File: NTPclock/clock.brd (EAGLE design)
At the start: 115 x 85 mm, 26 parts, among them IC1 MAX7219CNG

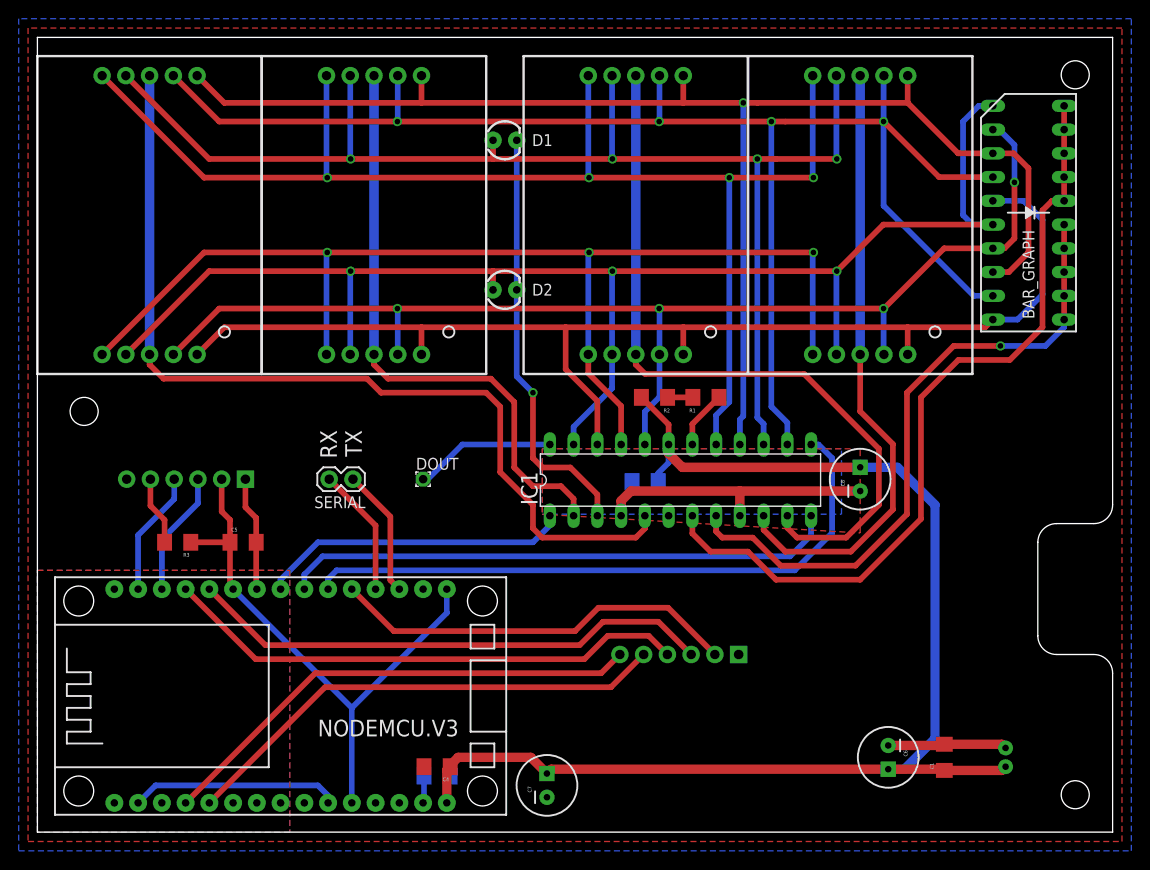
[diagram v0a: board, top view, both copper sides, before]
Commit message: Small power delivery improvements
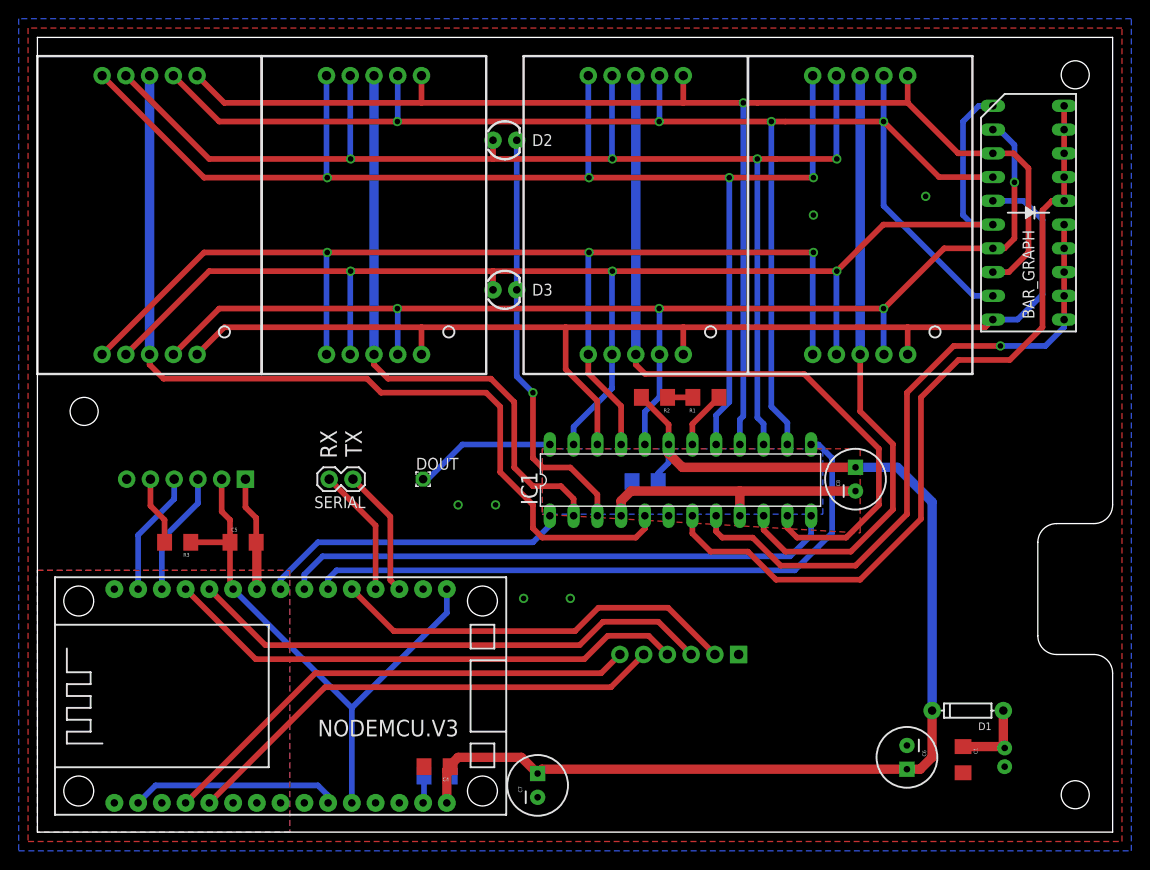
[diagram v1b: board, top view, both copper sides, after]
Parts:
- added D3: (no value), SparkFun-LED:LED3MM
- D1: device SparkFun-LED:LED3MM -> SparkFun-DiscreteSemi:DIODE-1N4148
- moved D1 78.6 mm to (99.5, 13.0), turned to 180 degrees
- moved D2 16.0 mm to (50.0, 74.0)
- moved C1 2.02 mm to (99.0, 7.75), turned to 270 degrees
- moved C6 2.00 mm to (93.0, 8.00)
- moved C7 1.00 mm to (53.5, 5.00)
- moved POWER 1.00 mm to (104.0, 8.00), turned to 90 degrees
- moved C8 0.50 mm to (87.5, 37.8)
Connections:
- net SQL renamed SQW
- new net VIN: C1.1, D1.A, POWER.2
- net D: now also D3.A; no longer D2.A
- net DIGIT4: now also D3.K; no longer D1.K
- net F: now also D2.A; no longer D1.A
- net VCC: now also D1.C; no longer C1.1, POWER.2
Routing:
- net GND: track 84.7 -> 71.4 mm, vias 0 -> 6
- net VCC: track 141.8 -> 129.8 mm
- net VIN: track 0.00 -> 8.57 mm
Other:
- board text added: "GND 3.3V SDA SCL SQW 32K"
- board text added: "GND D8 D4 D3 SD2 SD3"
- board text removed: "GND 3.3V SDA SCL SQL 32K"
- board text removed: "GND D8 D4 D3 SD1 SD2"

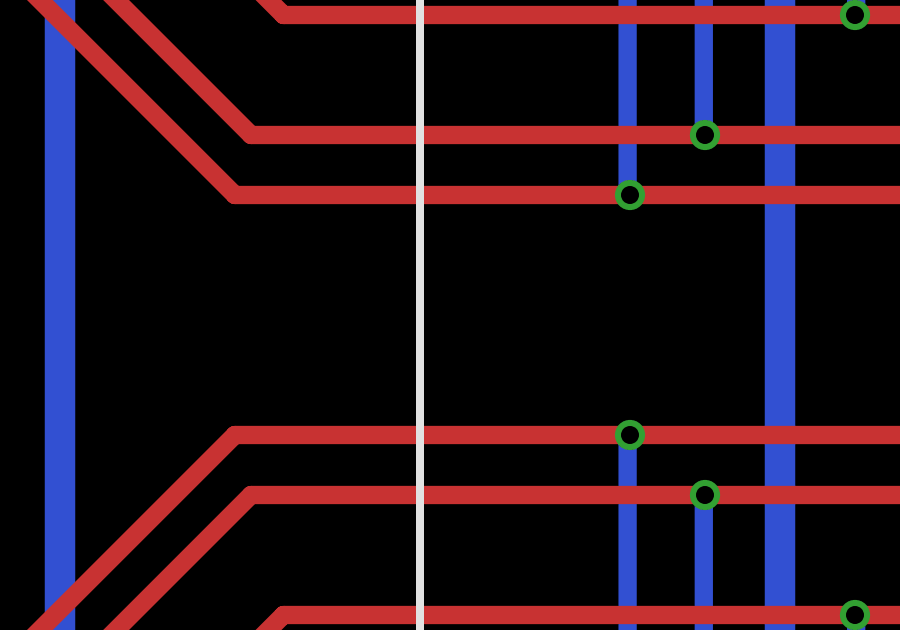
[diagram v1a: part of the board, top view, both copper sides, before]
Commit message: Added capacitor values
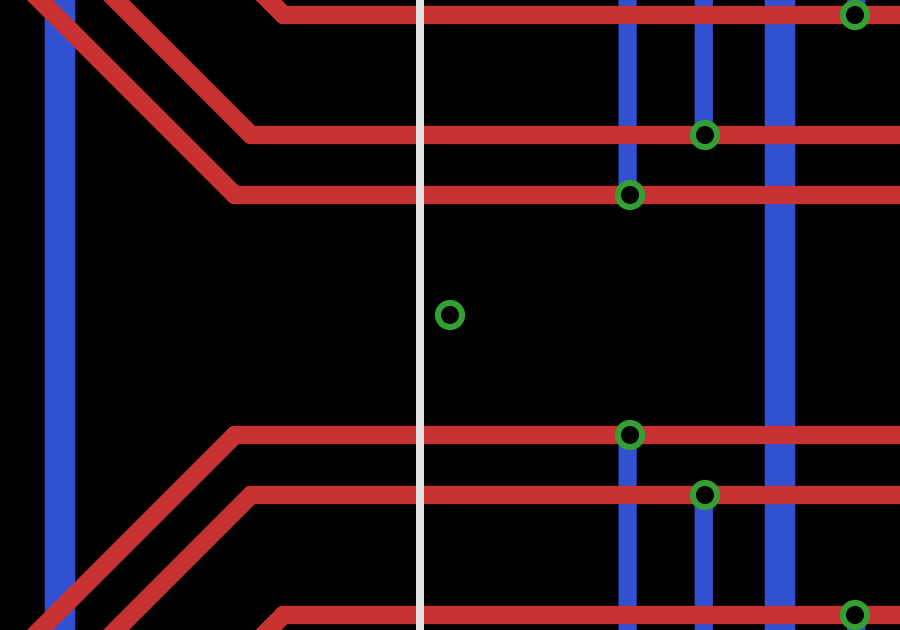
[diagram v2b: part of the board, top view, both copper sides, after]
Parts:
- C1, C4: value (none) -> 10μF
- C2: value (none) -> 0.1μF
- C5: value (none) -> 1mF
- C6: value 470μF -> 470mF
- C7: value (none) -> 330mF
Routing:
- net GND: vias 6 -> 7
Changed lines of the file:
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@@
 <attribute name="VALUE" x="67.397" y="48.024" size="0.4064" layer="27" rot="R180"/>
 </element>
-<element name="C1" library="SparkFun-Capacitors" package="1206" value="" x="99" y="7.75" rot="R270"/>
-<element name="C2" library="SparkFun-Capacitors" package="1206" value="" x="42.75" y="6" rot="MR0"/>
+<element name="C1" library="SparkFun-Capacitors" package="1206" value="10μF" x="99" y="7.75" rot="R270"/>
+<element name="C2" library="SparkFun-Capacitors" package="1206" value="0.1μF" x="42.75" y="6" rot="MR0"/>
 <element name="C3" library="SparkFun-Capacitors" package="1206" value="0.1μF" x="65" y="37.5" rot="MR0"/>
-<element name="C4" library="SparkFun-Capacitors" package="1206" value="" x="42.75" y="7" rot="R180"/>
-<element name="C5" library="SparkFun-Capacitors" package="1206" value="" x="22" y="31"/>
-<element name="C6" library="SparkFun-Capacitors" package="CPOL-RADIAL-100UF-25V" value="470μF" x="93" y="8" rot="R270"/>
-<element name="C7" library="SparkFun-Capacitors" package="CPOL-RADIAL-100UF-25V" value="" x="53.5" y="5" rot="R90"/>
+<element name="C4" library="SparkFun-Capacitors" package="1206" value="10μF" x="42.75" y="7" rot="R180"/>
+<element name="C5" library="SparkFun-Capacitors" package="1206" value="1mF" x="22" y="31"/>
+<element name="C6" library="SparkFun-Capacitors" package="CPOL-RADIAL-100UF-25V" value="470mF" x="93" y="8" rot="R270"/>
+<element name="C7" library="SparkFun-Capacitors" package="CPOL-RADIAL-100UF-25V" value="330mF" x="53.5" y="5" rot="R90"/>
 <element name="C8" library="SparkFun-Capacitors" package="CPOL-RADIAL-100UF-25V" value="10μF" x="87.5" y="37.75" rot="R90"/>
 <element name="POWER" library="SparkFun-Connectors" package="JST-2-PTH-VERT" value="" x="104" y="8" rot="MR90"/>
@@
 <wire x1="23.47" y1="25.99" x2="23.47" y2="30.93" width="1" layer="1"/>
 <wire x1="23.47" y1="30.93" x2="23.4" y2="31" width="1" layer="1"/>
+<via x="25" y="66" extent="1-16" drill="0.6"/>
 </signal>
 <signal name="ISET">

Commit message: Unit fixes
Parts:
- C6: value 470mF -> 470μF
- C7: value 330mF -> 47μF
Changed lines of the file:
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@@
 <element name="C4" library="SparkFun-Capacitors" package="1206" value="10μF" x="42.75" y="7" rot="R180"/>
 <element name="C5" library="SparkFun-Capacitors" package="1206" value="1mF" x="22" y="31"/>
-<element name="C6" library="SparkFun-Capacitors" package="CPOL-RADIAL-100UF-25V" value="470mF" x="93" y="8" rot="R270"/>
-<element name="C7" library="SparkFun-Capacitors" package="CPOL-RADIAL-100UF-25V" value="330mF" x="53.5" y="5" rot="R90"/>
+<element name="C6" library="SparkFun-Capacitors" package="CPOL-RADIAL-100UF-25V" value="470μF" x="93" y="8" rot="R270"/>
+<element name="C7" library="SparkFun-Capacitors" package="CPOL-RADIAL-100UF-25V" value="47μF" x="53.5" y="5" rot="R90"/>
 <element name="C8" library="SparkFun-Capacitors" package="CPOL-RADIAL-100UF-25V" value="10μF" x="87.5" y="37.75" rot="R90"/>
 <element name="POWER" library="SparkFun-Connectors" package="JST-2-PTH-VERT" value="" x="104" y="8" rot="MR90"/>

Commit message: Add v1.0 logo to board
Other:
- board text added: "NTPClock v1.0 'Rainbow Dash' Joshua Villwock, 2016/12"

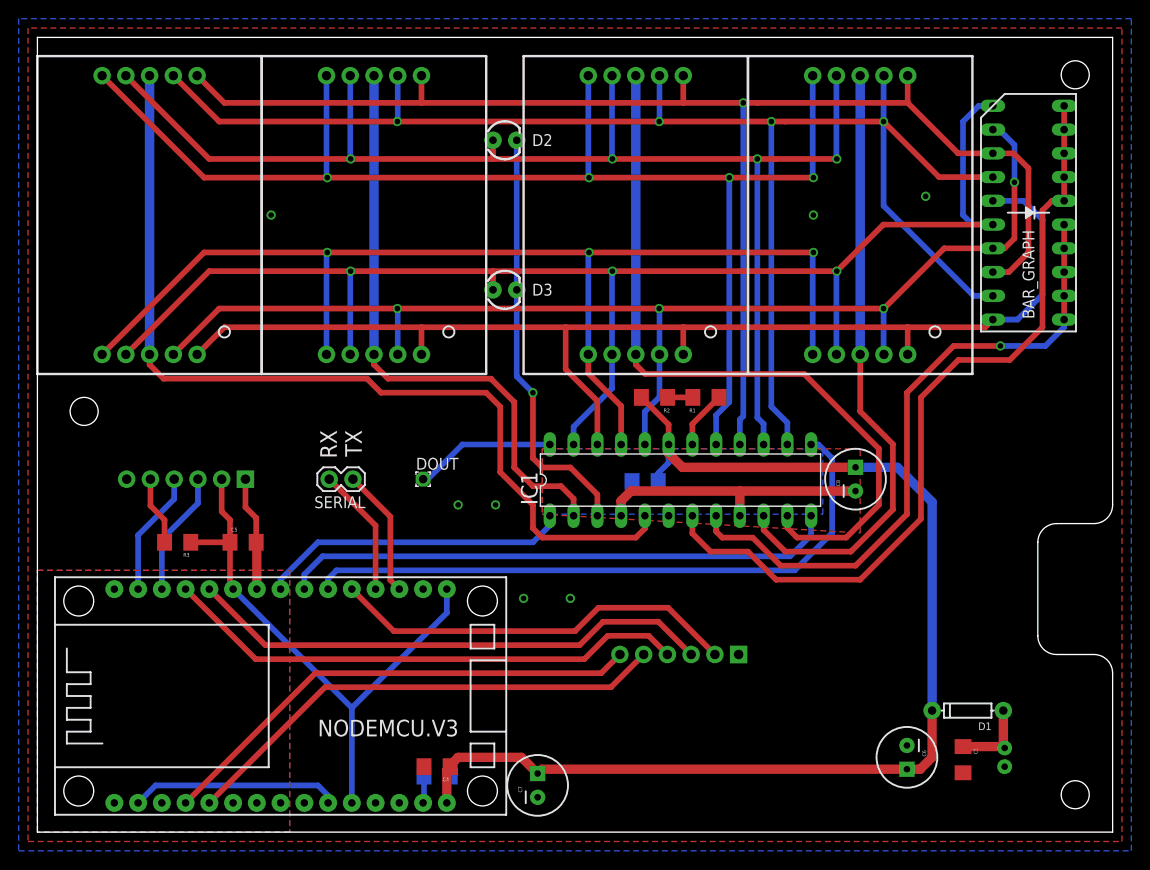
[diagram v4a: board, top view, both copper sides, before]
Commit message: Begin updating the Board file for the cheaper V3
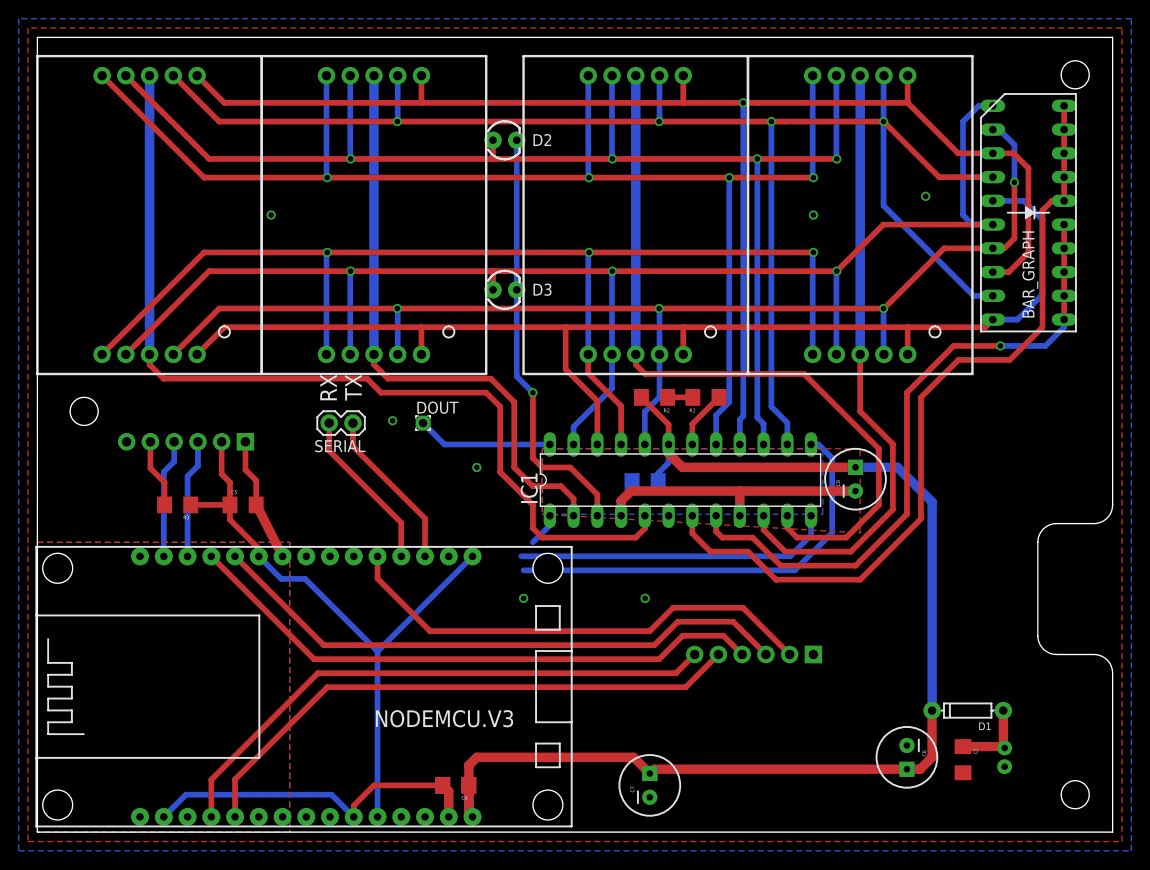
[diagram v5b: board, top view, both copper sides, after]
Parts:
- NODEMCU.V3: value ESP12E_DEVKIT -> ESP12E_V3_(WIDE); device NODEMCUv1:ESP12E_DEVKIT -> NODEMCUv1:ESP12E_V3_WIDE
- moved C7 12.0 mm to (65.5, 5.00)
- moved BUTTONS 8.00 mm to (83.0, 19.0)
- moved DOUT 6.00 mm to (41.2, 43.8)
- moved SERIAL 6.00 mm to (33.8, 43.8)
- moved NODEMCU.V3 4.12 mm to (30.0, 15.6)
- moved C5 4.00 mm to (22.0, 35.0)
- moved J0 4.00 mm to (22.2, 41.8)
- moved R3 4.00 mm to (15.0, 35.0)
- moved C4 2.83 mm to (44.8, 5.00)
- moved C2 2.24 mm to (44.8, 5.00)
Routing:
- net DATA: track 33.3 -> 3.59 mm
- net LOAD: track 59.6 -> 34.0 mm
- net CLK: track 67.9 -> 45.5 mm
- net GND: track 71.4 -> 84.8 mm
- net SD2: track 53.0 -> 61.2 mm
- net SD3: track 53.0 -> 61.2 mm
- net D8: track 43.8 -> 51.9 mm
- net D3: track 56.5 -> 63.2 mm
- net D4: track 56.5 -> 63.2 mm
- net 3.3V: track 61.5 -> 67.1 mm
- net TX: track 13.8 -> 17.5 mm
- net RX: track 13.8 -> 17.5 mm
- net SCL: track 13.4 -> 12.7 mm
- net SDA: track 13.4 -> 12.7 mm
- net DOUT: track 15.1 -> 14.5 mm

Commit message: Updated NTPclock for new footprint
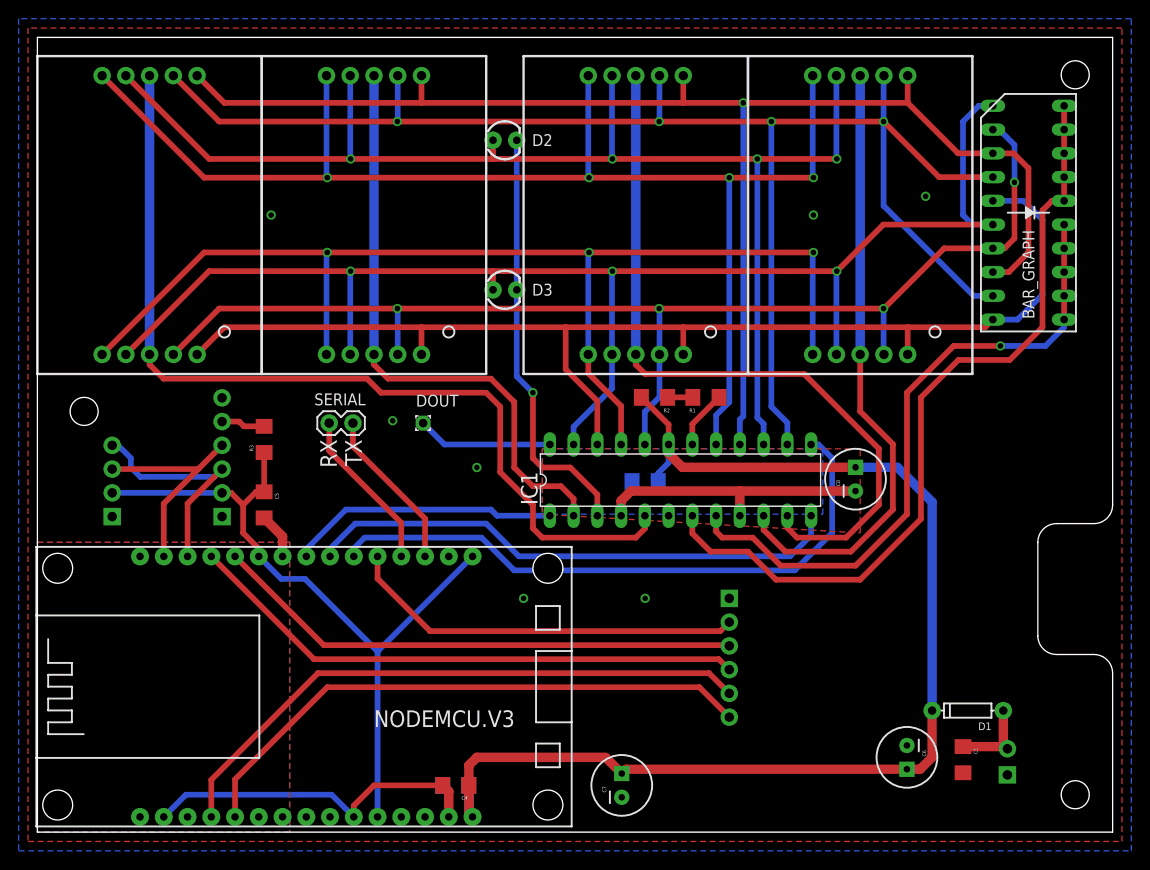
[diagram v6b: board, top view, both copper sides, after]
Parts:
- added J1: (no value), SparkFun-Connectors:MOLEX-1X4
- POWER: device SparkFun-Connectors:JST-2-PTH-VERT -> SparkFun-Connectors:MOLEX-1X2_LOCK
- moved R3 11.6 mm to (24.2, 42.0), turned to 90 degrees
- moved BUTTONS 10.8 mm to (74.0, 25.0), turned to 270 degrees
- moved J0 8.38 mm to (19.8, 33.8), turned to 90 degrees
- moved C7 3.00 mm to (62.5, 5.00)
- moved C5 2.25 mm to (24.2, 35.0), turned to 270 degrees
- moved POWER 1.77 mm to (103.8, 6.25)
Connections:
- net 3.3V: now also J1.2
- net GND: now also J1.1
- net SCL: now also J1.3
- net SD2: now also BUTTONS.6; no longer BUTTONS.5
- net SD3: now also BUTTONS.5; no longer BUTTONS.6
- net SDA: now also J1.4
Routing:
- net DATA: track 3.59 -> 28.8 mm
- net LOAD: track 34.0 -> 57.9 mm
- net CLK: track 45.5 -> 66.5 mm
- net SDA: track 12.7 -> 24.9 mm
- net SCL: track 12.7 -> 23.7 mm
- net 3.3V: track 67.1 -> 76.7 mm
- net D8: track 51.9 -> 42.7 mm
- net GND: track 84.8 -> 76.3 mm
- net D4: track 63.2 -> 56.8 mm
- net SD3: track 61.2 -> 65.0 mm
- net D3: track 63.2 -> 60.4 mm
- net SQW: track 7.38 -> 4.71 mm
- net SD2: track 61.2 -> 62.3 mm
- net VIN: track 8.57 -> 9.16 mm
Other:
- board text added: "32K SQW SCL SDA 3V3 GND"
- board text added: "GND D8 D4 D3 SD3 SD2"
- board text added: "NTPClock v1.3 'Rainbow Dash' Joshua Villwock, 2017/01"
- board text added: "SDA SCL 3V3 GND"
- board text removed: "GND 3.3V SDA SCL SQW 32K"
- board text removed: "GND D8 D4 D3 SD2 SD3"
- board text removed: "NTPClock v1.0 'Rainbow Dash' Joshua Villwock, 2016/12"
